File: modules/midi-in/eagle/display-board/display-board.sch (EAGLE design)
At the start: 21 parts

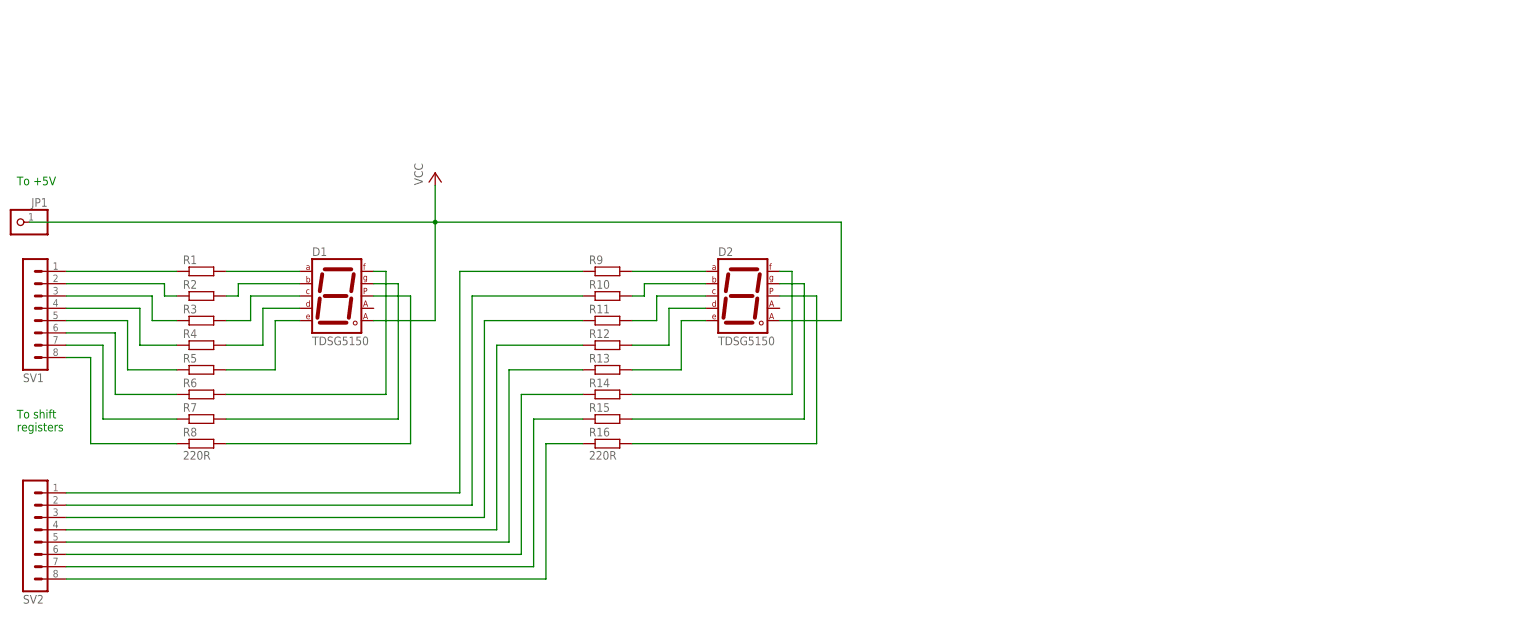
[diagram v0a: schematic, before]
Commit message: Added shift registers, start-up reset on display board schematic
TODO: revise the board, revise the main schematic
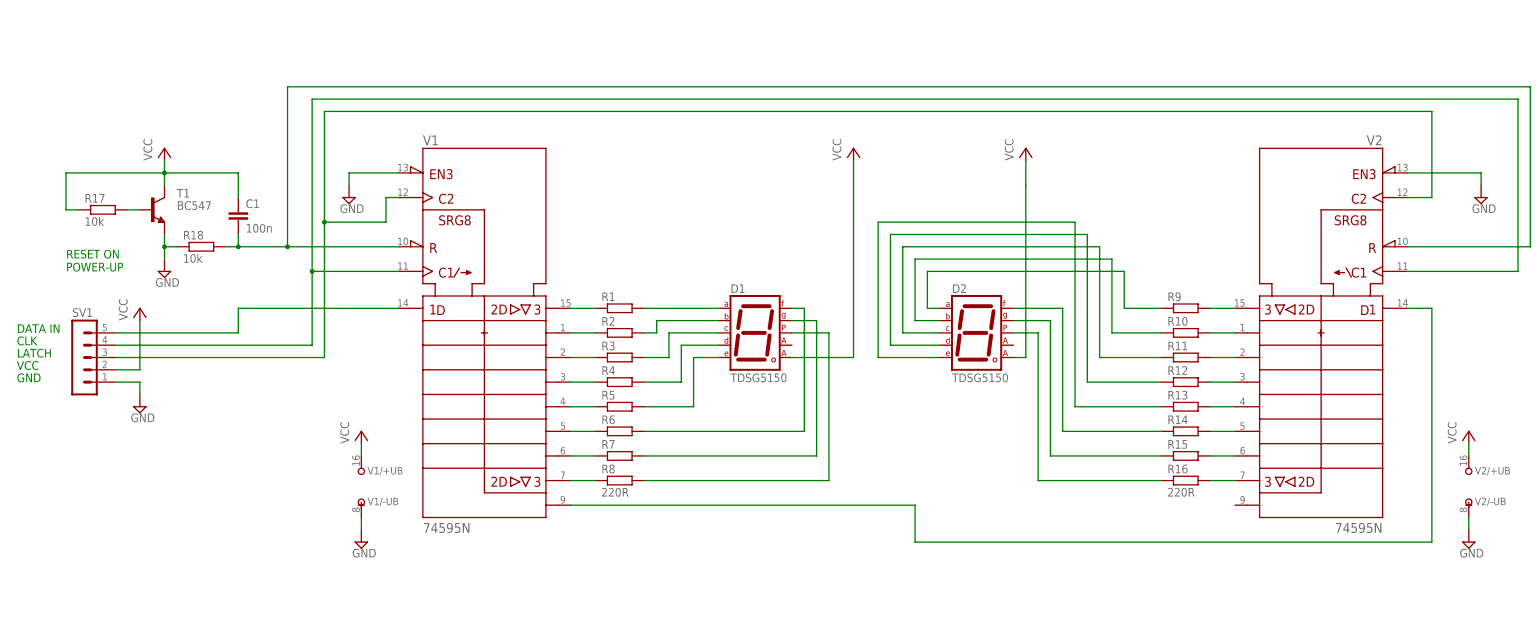
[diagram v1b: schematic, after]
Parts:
- removed JP1: (no value), pinhead:PINHD-1X1
- removed SV2: (no value), con-lstb:MA08-1
- added C1: 100n, rcl:C-EU050-024X044
- added R17, R18: 10k, resistor:R-EU_0207/7
- added T1: BC547, transistor:BC547
- added V1, V2: 74595N, 74ttl-din:74595N
- SV1: device con-lstb:MA08-1 -> con-lstb:MA05-1
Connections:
- new net GND: R18.1, SV1.1, T1.E, V1/-UB.-UB, V11.!G, V2/-UB.-UB, V21.!G
- new net N$33: V11.QH*, V21.SER
- new net N$34: C1.2, R18.2, V11.!SRCLR, V21.!SRCLR
- new net N$35: SV1.3, V11.RCK, V21.RCK
- new net N$36: SV1.4, V11.SRCK, V21.SRCK
- new net N$37: R17.2, T1.B
- new net N$38: SV1.5, V11.SER
- new net VCC1: D2.CA2
- net N$10: now also R10.1; no longer R10.2
- net N$11: now also R11.1; no longer R11.2
- net N$12: now also R12.1; no longer R12.2
- net N$13: now also R13.1; no longer R13.2
- net N$14: now also R14.1; no longer R14.2
- net N$15: now also R15.1; no longer R15.2
- net N$16: now also R16.1; no longer R16.2
- net N$17: now also V11.QA; no longer SV1.1
- net N$18: now also V11.QB; no longer SV1.2
- net N$19: now also V11.QC; no longer SV1.3
- net N$20: now also V11.QD; no longer SV1.4
- net N$21: now also V11.QE; no longer SV1.5
- net N$22: now also V11.QF; no longer SV1.6
- net N$23: now also V11.QG; no longer SV1.7
- net N$24: now also V11.QH; no longer SV1.8
- net N$25: now also R9.2, V21.QA; no longer R9.1, SV2.1
- net N$26: now also R10.2, V21.QB; no longer R10.1, SV2.2
- net N$27: now also R11.2, V21.QC; no longer R11.1, SV2.3
- net N$28: now also R12.2, V21.QD; no longer R12.1, SV2.4
- net N$29: now also R13.2, V21.QE; no longer R13.1, SV2.5
- net N$30: now also R14.2, V21.QF; no longer R14.1, SV2.6
- net N$31: now also R15.2, V21.QG; no longer R15.1, SV2.7
- net N$32: now also R16.2, V21.QH; no longer R16.1, SV2.8
- net N$9: now also R9.1; no longer R9.2
- net VCC: now also C1.1, R17.1, SV1.2, T1.C, V1/+UB.+UB, V2/+UB.+UB; no longer D2.CA2, JP1.1
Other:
- note added: "CLK"
- note added: "DATA IN"
- note added: "GND"
- note added: "LATCH"
- note added: "RESET ON POWER-UP"
- note added: "VCC"
- note removed: "To +5V"
- note removed: "To shift registers"
- moved on the sheet: D1, D2, R1, R10, R11, R12, R13, R14, R15, R16, R2, R3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

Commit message: Redesign display board layout w/ shift registers
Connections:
- net GND renamed N$46
- removed net VCC1: D2.CA2
- net VCC: now also D2.CA2
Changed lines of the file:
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@@
 <?xml version="1.0" encoding="utf-8"?>
 <!DOCTYPE eagle SYSTEM "eagle.dtd">
-<eagle version="7.5.0">
+<eagle version="7.3.0">
 <drawing>
 <settings>
@@
 <pinref part="P+6" gate="VCC" pin="VCC"/>
 </segment>
-</net>
-<net name="VCC1" class="0">
 <segment>
 <wire x1="213.36" y1="53.34" x2="213.36" y2="58.42" width="0.1524" layer="91"/>
@@
 </segment>
 </net>
-<net name="GND" class="0">
+<net name="N$46" class="0">
 <segment>
 <pinref part="V1" gate="/-UB" pin="-UB"/>

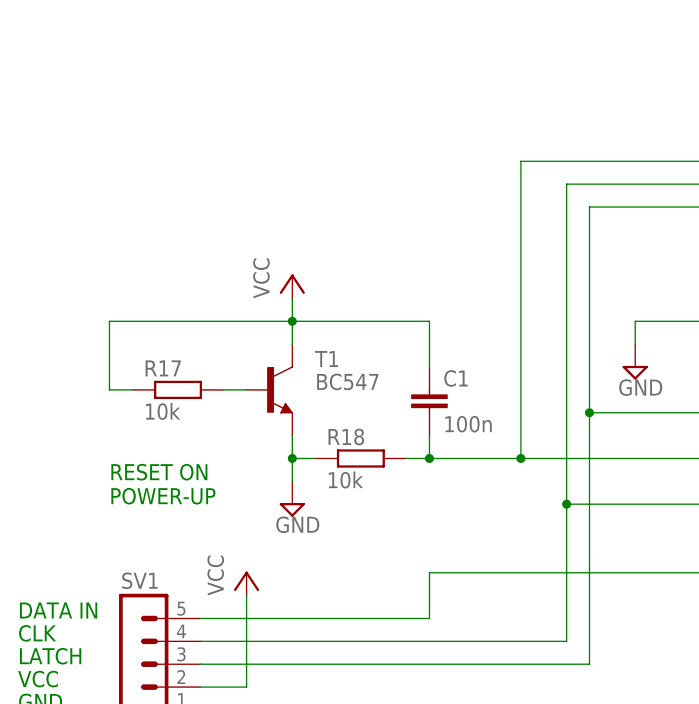
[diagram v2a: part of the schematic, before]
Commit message: Finish MIDI in display board and schematic, add readme
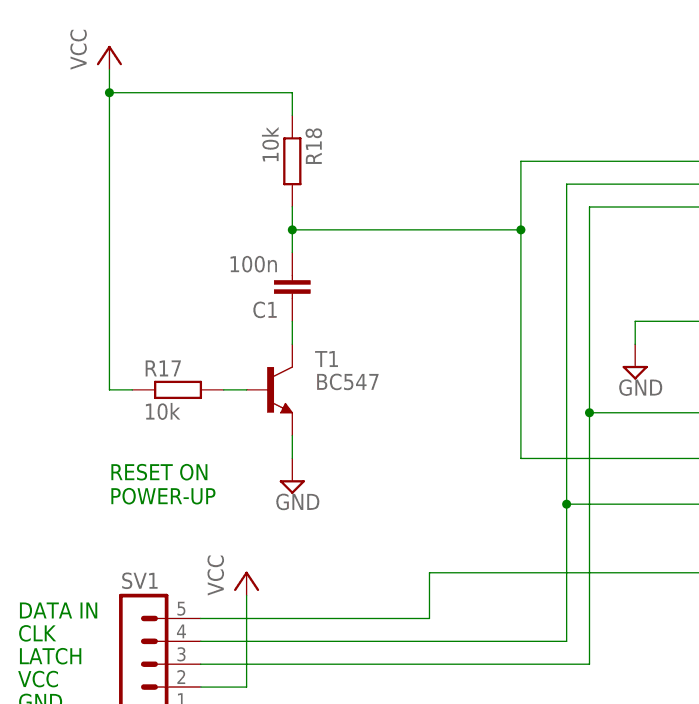
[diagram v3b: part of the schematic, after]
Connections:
- new net N$61: C1.1, T1.C
- net N$46: no longer R18.1
- net VCC: now also R18.1; no longer C1.1, T1.C
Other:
- moved on the sheet: C1, R18
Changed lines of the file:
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@@
 <?xml version="1.0" encoding="utf-8"?>
 <!DOCTYPE eagle SYSTEM "eagle.dtd">
-<eagle version="7.3.0">
+<eagle version="7.5.0">
 <drawing>
 <settings>
@@
 <attribute name="VALUE" x="19.05" y="80.518" size="1.778" layer="96"/>
 </instance>
-<instance part="R18" gate="G$1" x="43.18" y="76.2"/>
-<instance part="SUPPLY5" gate="GND" x="35.56" y="71.12"/>
-<instance part="C1" gate="G$1" x="50.8" y="83.82"/>
-<instance part="P+5" gate="VCC" x="35.56" y="96.52"/>
+<instance part="R18" gate="G$1" x="35.56" y="109.22" rot="R270"/>
+<instance part="SUPPLY5" gate="GND" x="35.56" y="73.66"/>
+<instance part="C1" gate="G$1" x="35.56" y="93.98" rot="R180"/>
+<instance part="P+5" gate="VCC" x="15.24" y="121.92"/>
 <instance part="SV1" gate="G$1" x="17.78" y="53.34"/>
 <instance part="P+6" gate="VCC" x="30.48" y="63.5"/>
@@
 </segment>
 <segment>
-<pinref part="C1" gate="G$1" pin="1"/>
-<wire x1="50.8" y1="86.36" x2="50.8" y2="91.44" width="0.1524" layer="91"/>
-<wire x1="50.8" y1="91.44" x2="35.56" y2="91.44" width="0.1524" layer="91"/>
-<pinref part="T1" gate="G$1" pin="C"/>
-<wire x1="35.56" y1="91.44" x2="35.56" y2="88.9" width="0.1524" layer="91"/>
-<wire x1="35.56" y1="91.44" x2="15.24" y2="91.44" width="0.1524" layer="91"/>
-<wire x1="15.24" y1="91.44" x2="15.24" y2="83.82" width="0.1524" layer="91"/>
-<pinref part="R17" gate="G$1" pin="1"/>
-<wire x1="15.24" y1="83.82" x2="17.78" y2="83.82" width="0.1524" layer="91"/>
-<junction x="35.56" y="91.44"/>
-<pinref part="P+5" gate="VCC" pin="VCC"/>
-<wire x1="35.56" y1="93.98" x2="35.56" y2="91.44" width="0.1524" layer="91"/>
-</segment>
-<segment>
 <pinref part="SV1" gate="G$1" pin="2"/>
 <wire x1="25.4" y1="50.8" x2="30.48" y2="50.8" width="0.1524" layer="91"/>
@@
 <wire x1="213.36" y1="88.9" x2="213.36" y2="93.98" width="0.1524" layer="91"/>
 <pinref part="P+2" gate="VCC" pin="VCC"/>
+</segment>
+<segment>
+<pinref part="R17" gate="G$1" pin="1"/>
+<wire x1="15.24" y1="119.38" x2="15.24" y2="116.84" width="0.1524" layer="91"/>
+<wire x1="15.24" y1="116.84" x2="15.24" y2="83.82" width="0.1524" layer="91"/>
+<wire x1="15.24" y1="83.82" x2="17.78" y2="83.82" width="0.1524" layer="91"/>
+<pinref part="P+5" gate="VCC" pin="VCC"/>
+<pinref part="R18" gate="G$1" pin="1"/>
+<wire x1="35.56" y1="114.3" x2="35.56" y2="116.84" width="0.1524" layer="91"/>
+<wire x1="35.56" y1="116.84" x2="15.24" y2="116.84" width="0.1524" layer="91"/>
+<junction x="15.24" y="116.84"/>
 </segment>
 </net>
@@
 <segment>
 <pinref part="SUPPLY5" gate="GND" pin="GND"/>
-<wire x1="35.56" y1="73.66" x2="35.56" y2="76.2" width="0.1524" layer="91"/>
 <pinref part="T1" gate="G$1" pin="E"/>
 <wire x1="35.56" y1="78.74" x2="35.56" y2="76.2" width="0.1524" layer="91"/>
-<pinref part="R18" gate="G$1" pin="1"/>
-<wire x1="35.56" y1="76.2" x2="38.1" y2="76.2" width="0.1524" layer="91"/>
-<junction x="35.56" y="76.2"/>
 </segment>
 <segment>
@@
 <segment>
 <pinref part="R18" gate="G$1" pin="2"/>
-<pinref part="C1" gate="G$1" pin="2"/>
-<wire x1="48.26" y1="76.2" x2="50.8" y2="76.2" width="0.1524" layer="91"/>
-<wire x1="50.8" y1="76.2" x2="50.8" y2="78.74" width="0.1524" layer="91"/>
 <pinref part="V1" gate="1" pin="!SRCLR"/>
-<wire x1="50.8" y1="76.2" x2="60.96" y2="76.2" width="0.1524" layer="91"/>
-<junction x="50.8" y="76.2"/>
 <wire x1="60.96" y1="76.2" x2="83.82" y2="76.2" width="0.1524" layer="91"/>
-<wire x1="60.96" y1="76.2" x2="60.96" y2="109.22" width="0.1524" layer="91"/>
+<wire x1="60.96" y1="76.2" x2="60.96" y2="101.6" width="0.1524" layer="91"/>
+<wire x1="60.96" y1="101.6" x2="60.96" y2="109.22" width="0.1524" layer="91"/>
 <wire x1="60.96" y1="109.22" x2="317.5" y2="109.22" width="0.1524" layer="91"/>
 <wire x1="317.5" y1="109.22" x2="317.5" y2="76.2" width="0.1524" layer="91"/>
 <pinref part="V2" gate="1" pin="!SRCLR"/>
 <wire x1="317.5" y1="76.2" x2="292.1" y2="76.2" width="0.1524" layer="91"/>
-<junction x="60.96" y="76.2"/>
+<pinref part="C1" gate="G$1" pin="2"/>
+<wire x1="35.56" y1="104.14" x2="35.56" y2="101.6" width="0.1524" layer="91"/>
+<wire x1="35.56" y1="101.6" x2="35.56" y2="99.06" width="0.1524" layer="91"/>
+<wire x1="35.56" y1="101.6" x2="60.96" y2="101.6" width="0.1524" layer="91"/>
+<junction x="60.96" y="101.6"/>
+<junction x="35.56" y="101.6"/>
 </segment>
 </net>
@@
 </segment>
 </net>
+<net name="N$61" class="0">
+<segment>
+<pinref part="C1" gate="G$1" pin="1"/>
+<pinref part="T1" gate="G$1" pin="C"/>
+<wire x1="35.56" y1="91.44" x2="35.56" y2="88.9" width="0.1524" layer="91"/>
+</segment>
+</net>
